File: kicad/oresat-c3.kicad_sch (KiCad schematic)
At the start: 0 parts

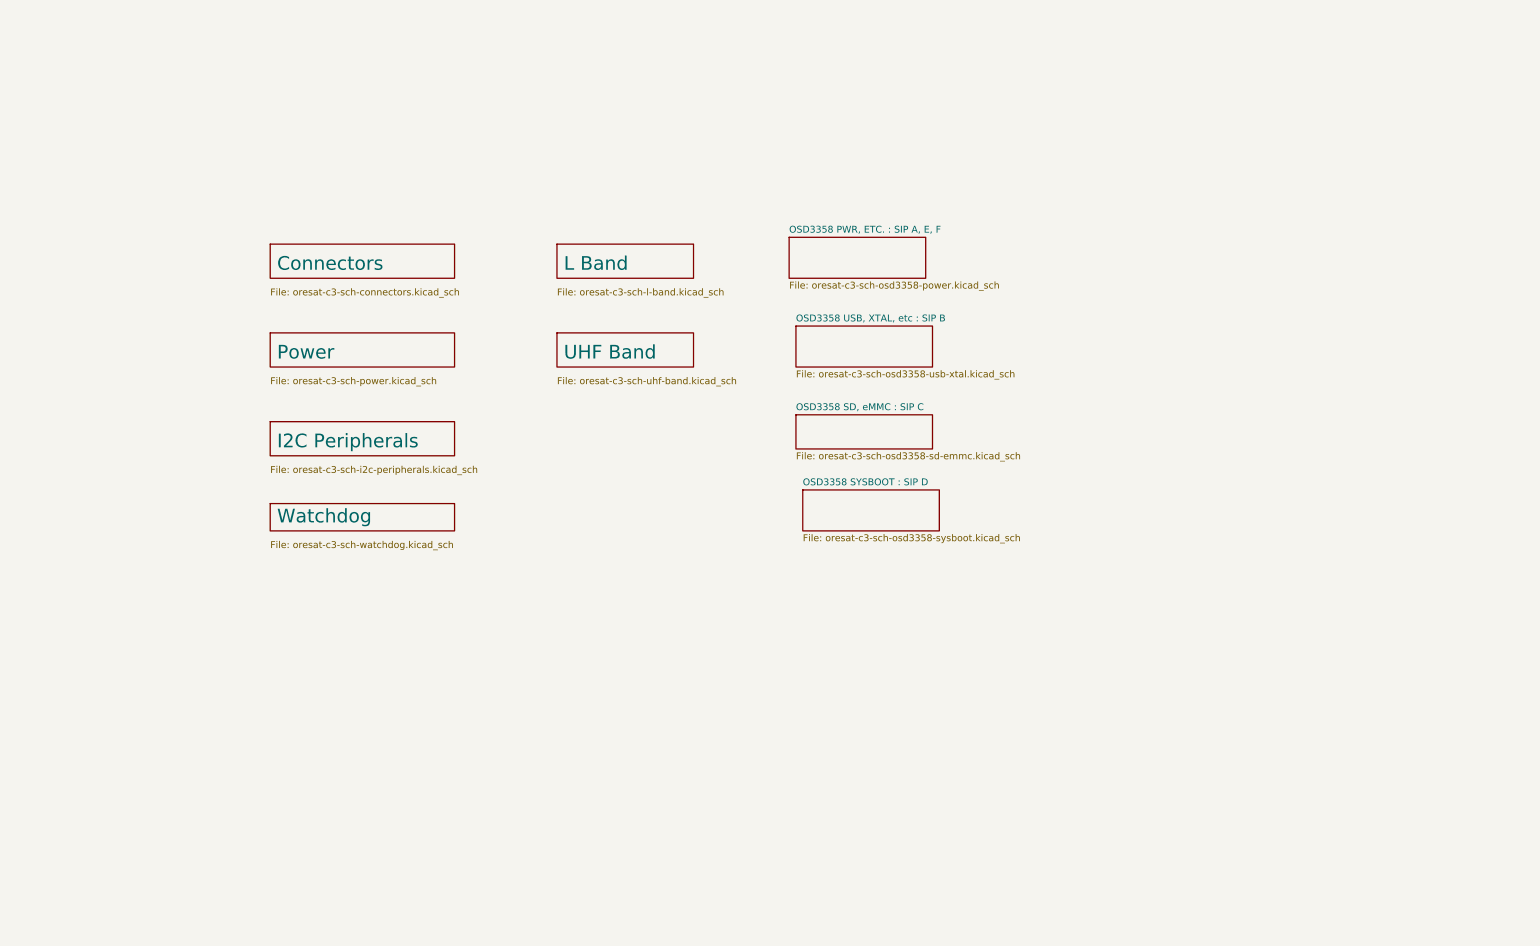
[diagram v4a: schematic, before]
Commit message: C3 v6 schematic now 80% done. OSD2258 IC has been gone over with a fine tooth comb and simplified as much as possible. OSD3358 pinout compared to RED board and PocketBeagle. What's left: lots of little issues, footprints, and then L band and UHF radio schematics need to be fixed.
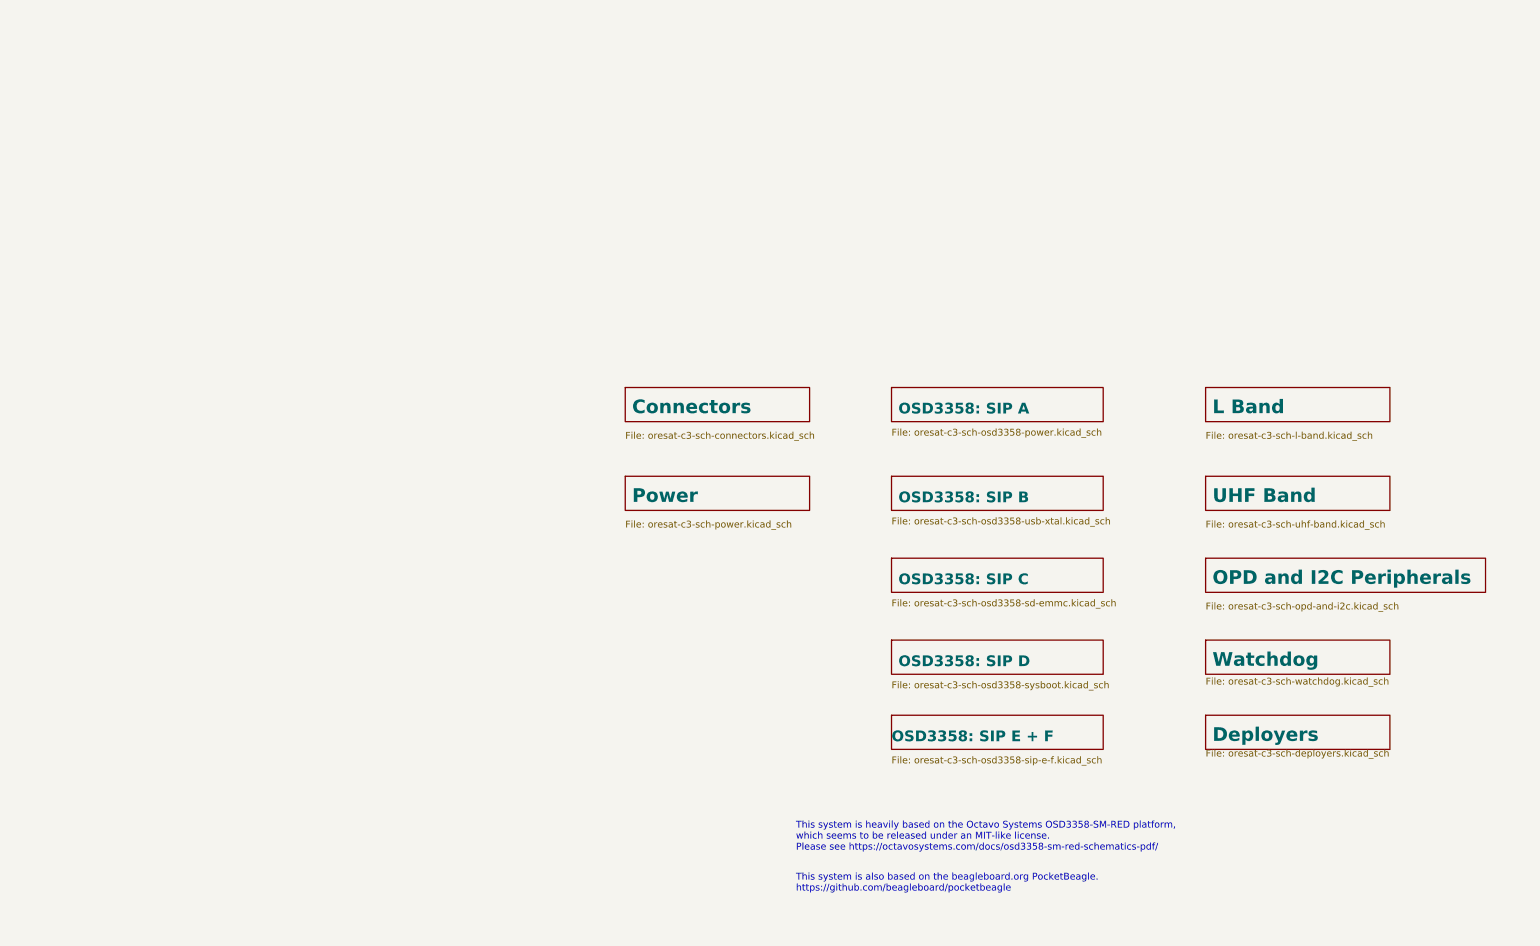
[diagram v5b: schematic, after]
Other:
- sheet I2C Peripherals renamed OPD and I2C Peripherals
- sheet OSD3358 PWR, ETC. : SIP A, E, F renamed OSD3358: SIP A
- sheet OSD3358 SD, eMMC : SIP C renamed OSD3358: SIP C
- sheet OSD3358 SYSBOOT : SIP D renamed OSD3358: SIP D
- sheet OSD3358 USB, XTAL, etc : SIP B renamed OSD3358: SIP B
- added sheet Deployers (oresat-c3-sch-deployers.kicad_sch)
- added sheet OSD3358: SIP E + F (oresat-c3-sch-osd3358-sip-e-f.kicad_sch)
- sheet OPD and I2C Peripherals: file oresat-c3-sch-i2c-peripherals.kicad_sch -> oresat-c3-sch-opd-and-i2c.kicad_sch
- note added: "This system is also based on the beagleboard.org PocketBeagle. https://github.com/beagleboard/pocketbeagle"
- note added: "This system is heavily based on the Octavo Systems OSD3358-SM-RED platform, which seems to be released under an MIT-like license. Please see https://octavosystems.com/docs/osd3358-sm-red-schematics-pdf/"
- title: (none) -> OreSat C3 Root Schematic

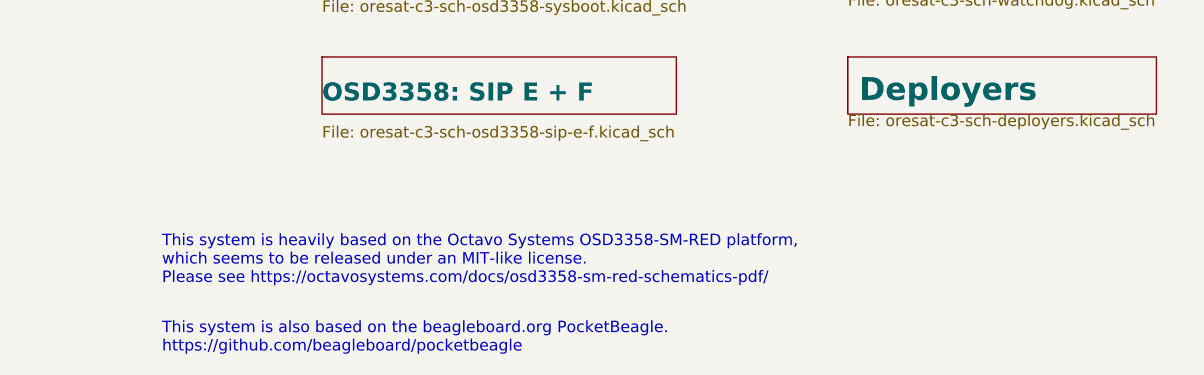
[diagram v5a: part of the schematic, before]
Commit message: Rough draft schematic of C3 v6 done. L band fixed, some GPIO attached, awaiting design review before final attachments.
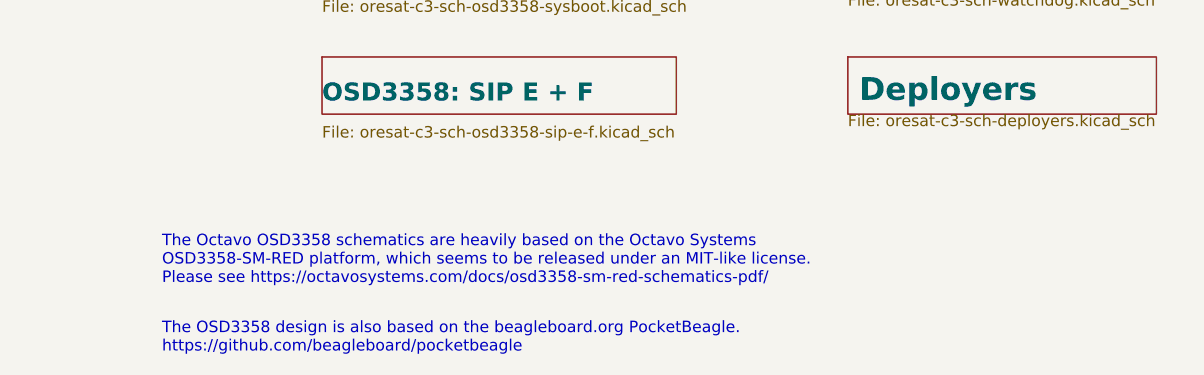
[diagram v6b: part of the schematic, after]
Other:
- note added: "The OSD3358 design is also based on the beagleboard.org PocketBeagle. https://github.com/beagleboard/pocketbeagle"
- note added: "The Octavo OSD3358 schematics are heavily based on the Octavo Systems OSD3358-SM-RED platform, which seems to be released under an MIT-like license. Please see https://octavosystems.com/docs/osd3358-sm-red-schematics-pdf/"
- note removed: "This system is also based on the beagleboard.org PocketBeagle. https://github.com/beagleboard/pocketbeagle"
- note removed: "This system is heavily based on the Octavo Systems OSD3358-SM-RED platform, which seems to be released under an MIT-like license. Please see https://octavosystems.com/docs/osd3358-sm-red-schematics-pdf/"
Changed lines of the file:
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@@
     (rev "6.0")
   )
-  (text "This system is heavily based on the Octavo Systems OSD3358-SM-RED platform,\nwhich seems to be released under an MIT-like license.\nPlease see https://octavosystems.com/docs/osd3358-sm-red-schematics-pdf/\n"
+  (text "The Octavo OSD3358 schematics are heavily based on the Octavo Systems \nOSD3358-SM-RED platform, which seems to be released under an MIT-like license.\nPlease see https://octavosystems.com/docs/osd3358-sm-red-schematics-pdf/\n"
     (at 171.45 179.07 0)
     (effects (font (size 1.27 1.27)) (justify left bottom))
   )
-  (text "This system is also based on the beagleboard.org PocketBeagle.\nhttps://github.com/beagleboard/pocketbeagle"
+  (text "The OSD3358 design is also based on the beagleboard.org PocketBeagle.\nhttps://github.com/beagleboard/pocketbeagle"
     (at 171.45 186.69 0)
     (effects (font (size 1.27 1.27)) (justify left bottom))

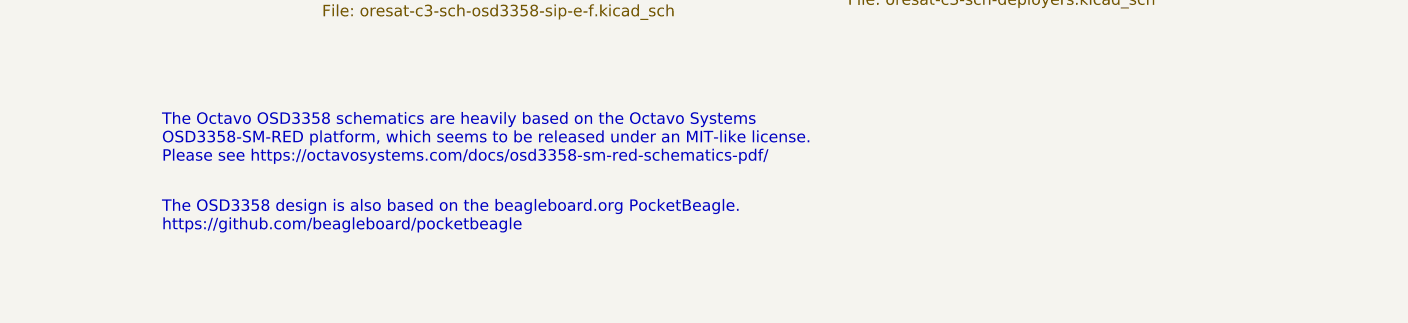
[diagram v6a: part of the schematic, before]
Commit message: Fixed R82 so that the damn thing doesn't reboot every two seconds. Fixed R63 to extend the watchdog timer. Fixed R83 and R84 in order to set the UVLO correctly.
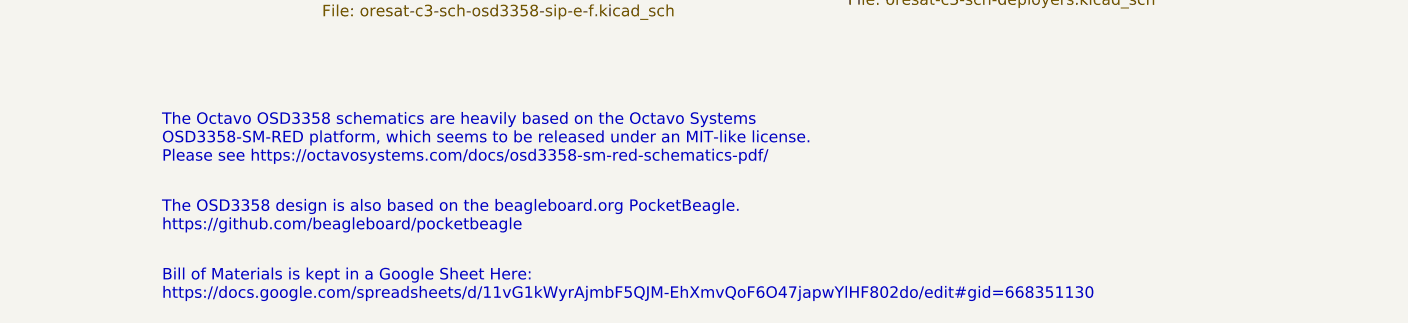
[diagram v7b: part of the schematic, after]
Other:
- note added: "Bill of Materials is kept in a Google Sheet Here: https://docs.google.com/spreadsheets/d/11vG1kWyrAjmbF5QJM-EhXmvQoF6O47japwYlHF802do/edit#gid=668351130"
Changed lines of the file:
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@@
     (rev "6.0")
+  )
+  (text "Bill of Materials is kept in a Google Sheet Here:\nhttps://docs.google.com/spreadsheets/d/11vG1kWyrAjmbF5QJM-EhXmvQoF6O47japwYlHF802do/edit#gid=668351130"
+    (at 171.45 194.31 0)
+    (effects (font (size 1.27 1.27)) (justify left bottom))
   )
   (text "The Octavo OSD3358 schematics are heavily based on the Octavo Systems \nOSD3358-SM-RED platform, which seems to be released under an MIT-like license.\nPlease see https://octavosystems.com/docs/osd3358-sm-red-schematics-pdf/\n"
